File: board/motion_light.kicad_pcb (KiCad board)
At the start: 2 copper layers, 35 x 64 mm, 24 parts, among them CON1 AVR-ISP-6, J1 MOTION, J2 Conn_01x05, J3 USB_MICRO, J4 USB_MICRO, Q1 BSS83P, SW1 SW_Push, SW2 SW_Push, U1 ATTINY84A-SSU, U2 APA102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

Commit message: Add separate power control for motion detector power
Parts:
- added Q2: BSS83P, Package_TO_SOT_SMD:SOT-23, F.Cu at (132.5, 83.0)
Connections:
- J1 pad 2: /ACC_PWR -> /MOT_PWR
- J2 pad 3: /PA7 -> /MOT_PWR
- J3 pad 2: Net-(J3-Pad2) -> (no net)
- J3 pad 3: Net-(J3-Pad3) -> (no net)
- J3 pad 4: Net-(J3-Pad4) -> (no net)
- J4 pad 2: Net-(J4-Pad2) -> (no net)
- J4 pad 3: Net-(J4-Pad3) -> (no net)
- J4 pad 4: Net-(J4-Pad4) -> (no net)
- U1 pad 6: /PA7 -> /~MOT_PWR_EN
- U3 pad 5: Net-(U3-Pad5) -> (no net)
- U3 pad 6: Net-(U3-Pad6) -> (no net)
- U4 pad 1: /ACC_PWR -> /MOT_PWR
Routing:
- net /MOT_PWR: track 0.00 -> 49.0 mm, vias 0 -> 2
- net /ACC_PWR: track 71.1 -> 49.3 mm, vias 3 -> 2
- net /PA7: track 14.1 -> 0.00 mm
- net /STATUS_LED: track 41.1 -> 32.0 mm
- net /~MOT_PWR_EN: track 0.00 -> 6.47 mm
- net /BUTTON2: track 38.1 -> 33.5 mm, vias 1 -> 0
- net /MOTION: track 47.3 -> 45.8 mm, vias 4 -> 5
- net VCC: track 11.5 -> 10.3 mm
- net Net-(D1-Pad1): track 11.0 -> 11.8 mm
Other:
- board text added: "ACC_P"
- board text added: "MOT_P"
- board text added: "Motion Night Light 2018 Steve Pomeroy staticfree.info Version 1.2.0"
- board text removed: "Motion Night Light 2018 Steve Pomeroy staticfree.info Version 1.1.0"
- board text removed: "PA3"
- board text removed: "PA7"

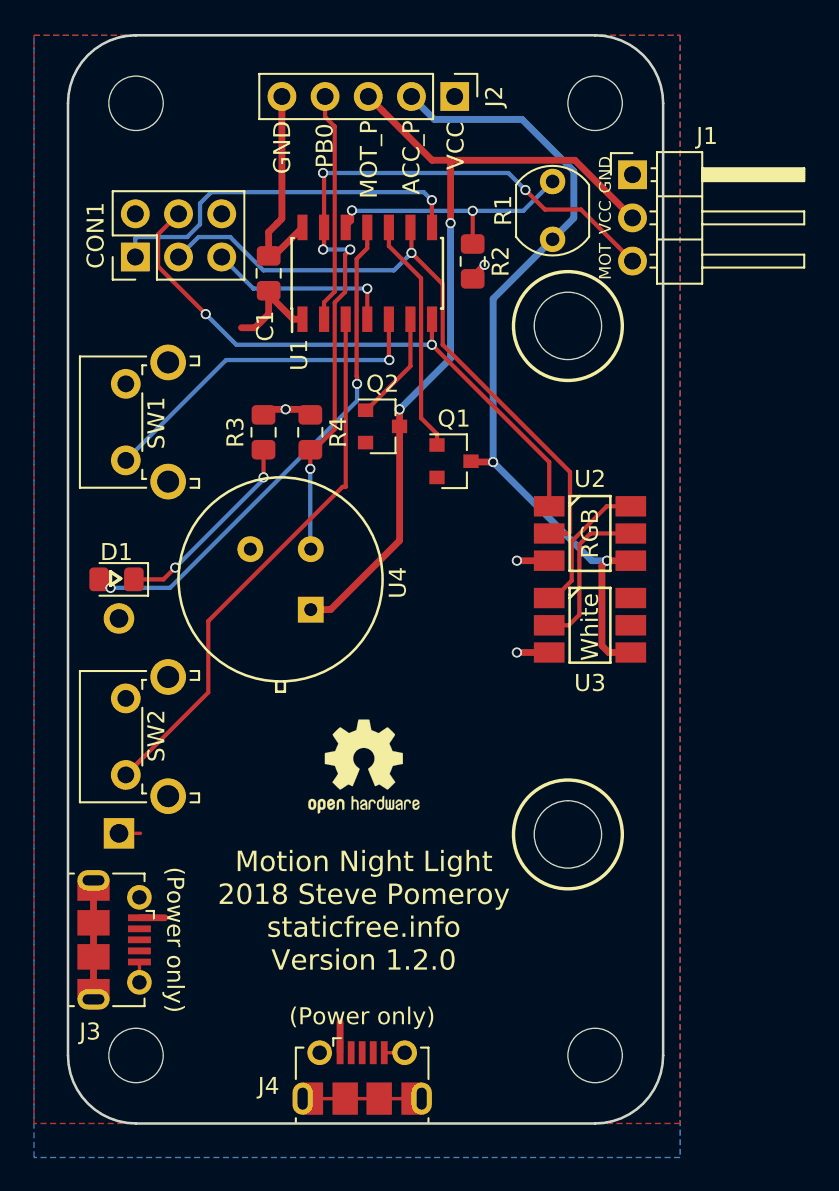
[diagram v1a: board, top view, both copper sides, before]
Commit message: Rotate motion detector to work with wall-oriented detector
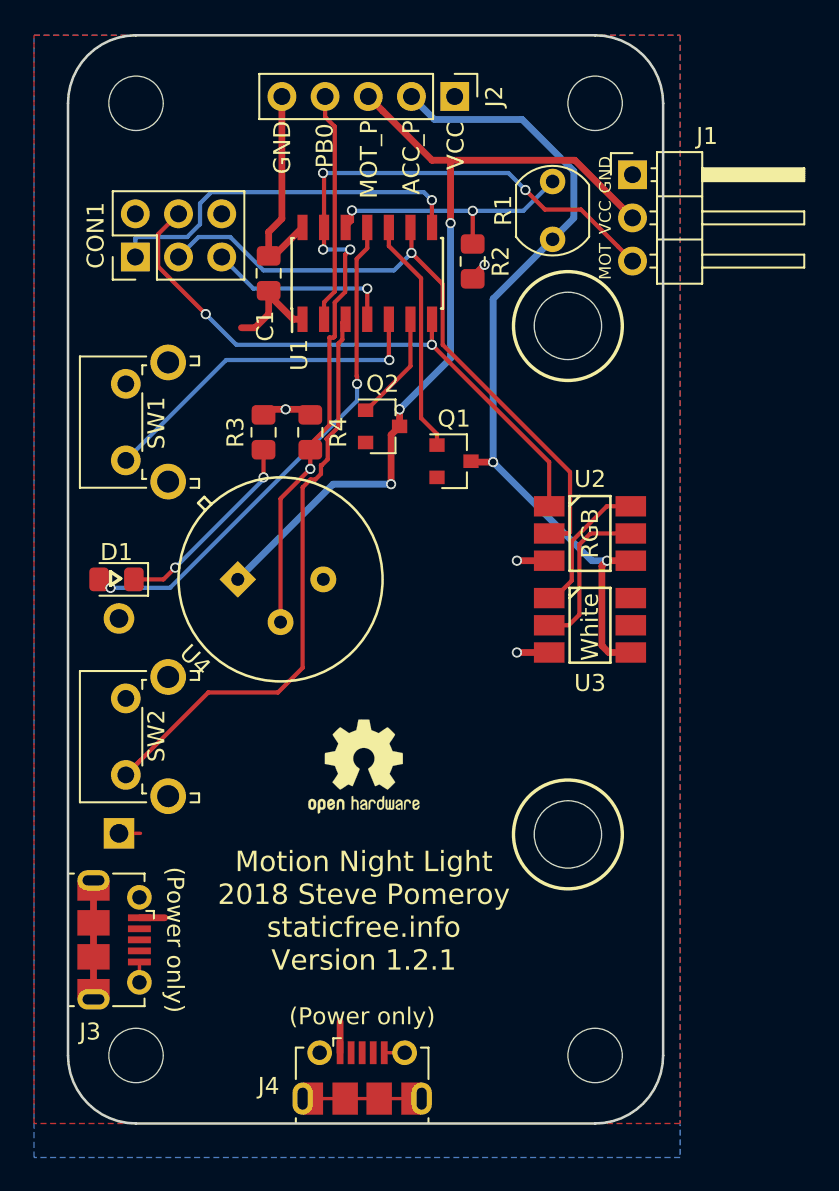
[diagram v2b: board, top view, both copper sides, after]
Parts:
- turned U4 to 315 degrees
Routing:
- net /MOTION: track 45.8 -> 50.9 mm
- net /BUTTON2: track 33.5 -> 36.1 mm
- net /MOT_PWR: track 49.0 -> 50.3 mm, vias 2 -> 3
- net GND: track 35.6 -> 34.9 mm
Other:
- board text added: "Motion Night Light 2018 Steve Pomeroy staticfree.info Version 1.2.1"
- board text removed: "Motion Night Light 2018 Steve Pomeroy staticfree.info Version 1.2.0"

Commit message: Update with new resistor value
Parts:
- R2: value 10K -> 100K
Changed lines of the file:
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@@
-(kicad_pcb (version 20171130) (host pcbnew 5.0.1+dfsg1-3)
+(kicad_pcb (version 20171130) (host pcbnew 5.0.2+dfsg1-1)
   (general
     (thickness 1.6)
@@
       (effects (font (size 1 1) (thickness 0.15)))
     )
-    (fp_text value 10K (at 0 -1.7 270) (layer F.Fab)
-      (effects (font (size 1 1) (thickness 0.15)))
-    )
+    (fp_text value 100K (at 0 -1.7 270) (layer F.Fab)
+      (effects (font (size 1 1) (thickness 0.15)))
+    )

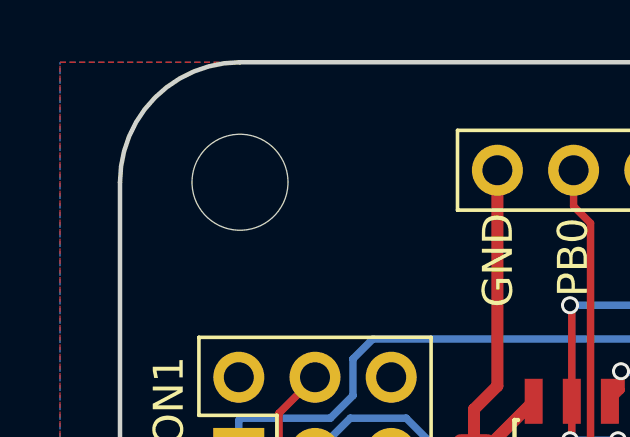
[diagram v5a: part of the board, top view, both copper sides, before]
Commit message: Update to KiCAD 5.1
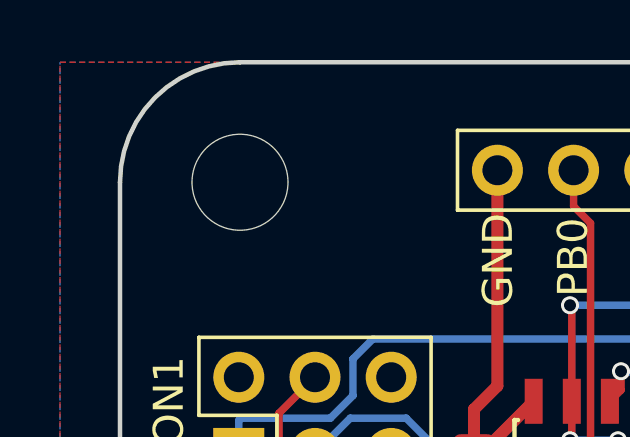
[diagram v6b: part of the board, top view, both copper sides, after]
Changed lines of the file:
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@@
-(kicad_pcb (version 20171130) (host pcbnew 5.0.2+dfsg1-1)
+(kicad_pcb (version 20171130) (host pcbnew 5.1.4+dfsg1-1)
   (general
     (thickness 1.6)
@@
     (zone_45_only no)
     (trace_min 0.2)
-    (segment_width 0.2)
-    (edge_width 0.2)
     (via_size 0.6)
     (via_drill 0.4)
@@
     (uvia_min_size 0.2)
     (uvia_min_drill 0.1)
+    (edge_width 0.2)
+    (segment_width 0.2)
     (pcb_text_width 0.3)
     (pcb_text_size 1.5 1.5)
@@
   (gr_arc (start 118 120) (end 118 124) (angle 90) (layer Edge.Cuts) (width 0.15))
   (gr_arc (start 145 64) (end 145 60) (angle 90) (layer Edge.Cuts) (width 0.15))
-  (gr_arc (start 118 64) (end 114 64) (angle 89.9) (layer Edge.Cuts) (width 0.15))
+  (gr_arc (start 118 64) (end 114 64) (angle 90) (layer Edge.Cuts) (width 0.15))
   (gr_text "(Power only)" (at 120.3 113.2 270) (layer F.SilkS)
     (effects (font (size 1 1) (thickness 0.2)))
